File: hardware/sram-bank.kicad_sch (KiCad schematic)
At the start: 13 parts, among them U1 74LVC138A, U13 74LVC138A

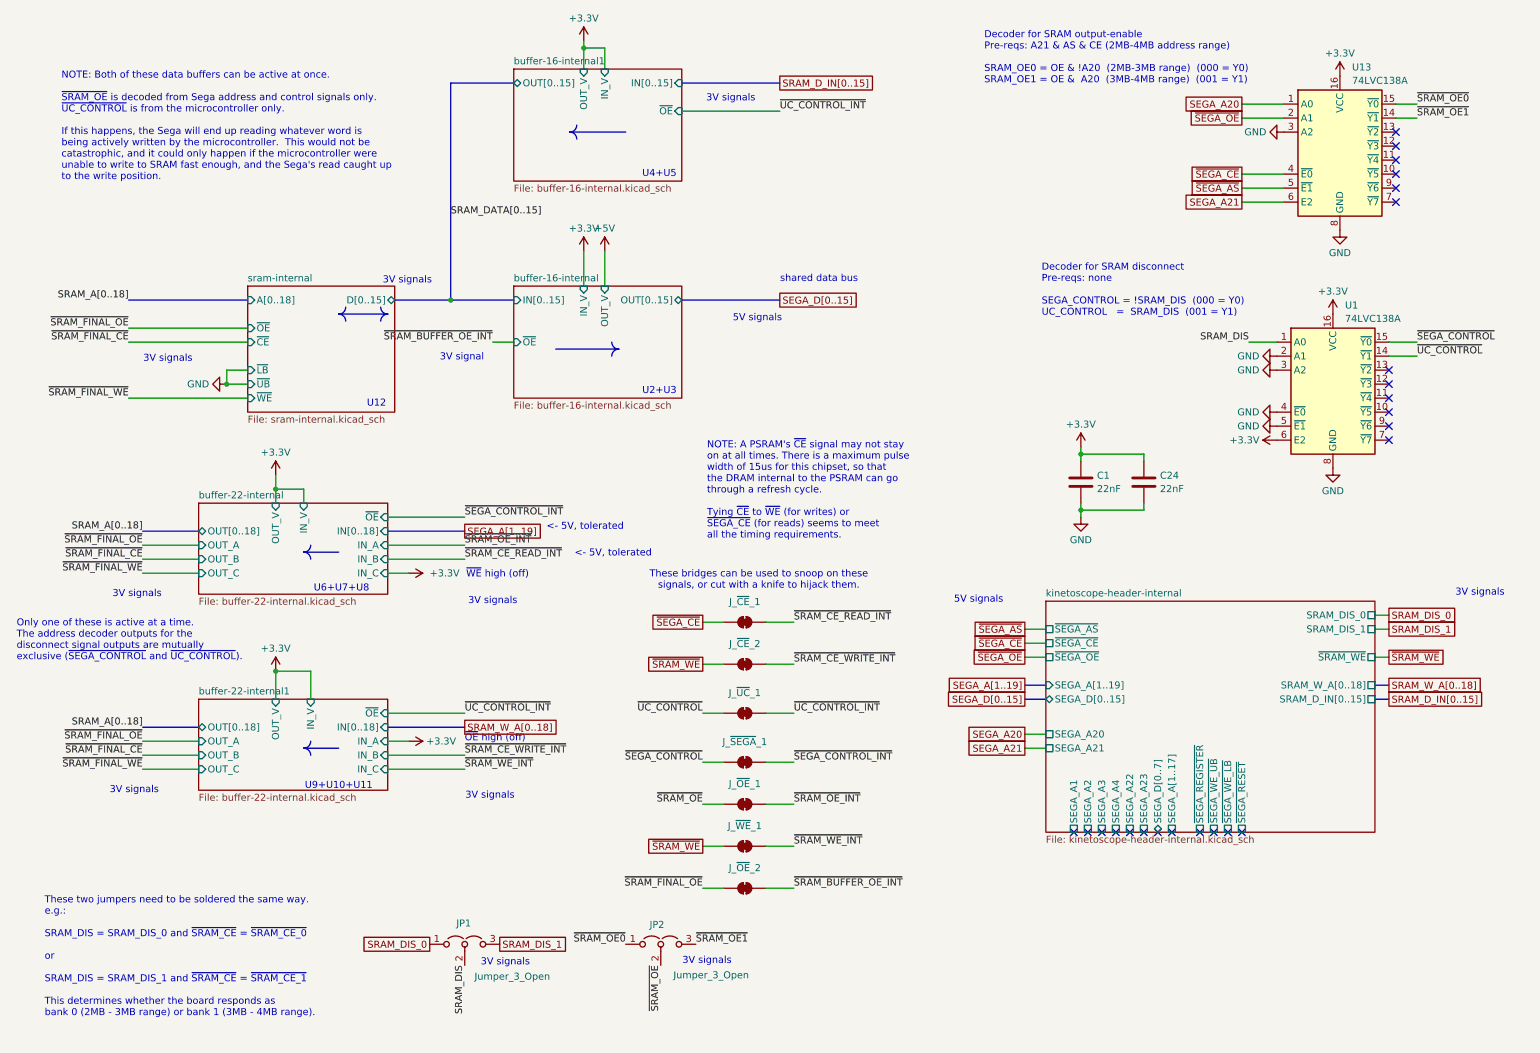
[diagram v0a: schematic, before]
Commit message: Move SRAM bank board design into shareable subsheet
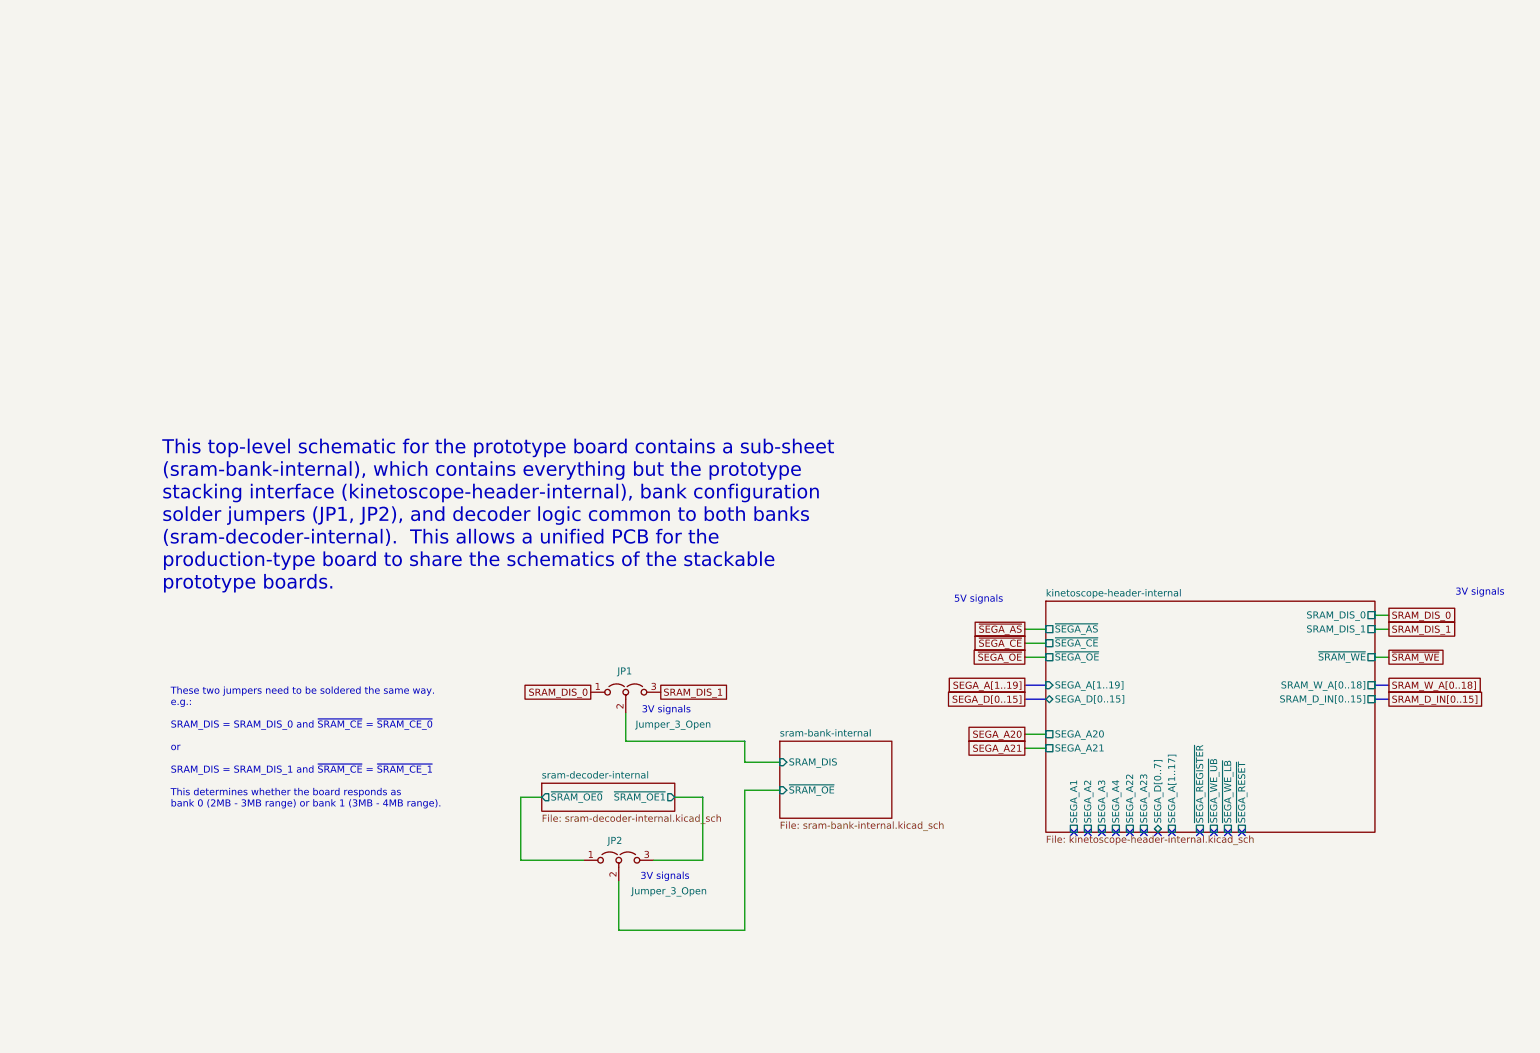
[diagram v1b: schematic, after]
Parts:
- removed C1, C24: 22nF, Capacitor_SMD:C_0603_1608Metric, symbol Device:C
- removed J_~{CE}_1, J_~{CE}_2, J_~{OE}_1, J_~{OE}_2, J_~{SEGA}_1, J_~{UC}_1, J_~{WE}_1: ~, Jumper:SolderJumper-2_P1.3mm_Bridged_RoundedPad1.0x1.5mm, symbol Jumper:SolderJumper_2_Bridged
- removed U1, U13: 74LVC138A, Package_SO:TSSOP-16_4.4x5mm_P0.65mm, symbol 74xx:74HC138
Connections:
- net SRAM_DIS renamed sram-bank-internal/SRAM_DIS
- net ~{SRAM_OE0} renamed sram-decoder-internal/~{SRAM_OE0}
- net ~{SRAM_OE1} renamed sram-decoder-internal/~{SRAM_OE1}
- net ~{SRAM_OE} renamed sram-bank-internal/~{SRAM_OE}
- no-connect marks 24 -> 12
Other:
- removed sheet buffer-16-internal
- removed sheet buffer-16-internal1
- removed sheet buffer-22-internal
- removed sheet buffer-22-internal1
- removed sheet sram-internal
- added sheet sram-bank-internal (sram-bank-internal.kicad_sch)
- added sheet sram-decoder-internal (sram-decoder-internal.kicad_sch)
- note added: "This top-level schematic for the prototype board contains a sub-sheet (sram-bank-internal), which contains everything but the prototype stacking interface (kinetoscope-header-internal), bank configuration solder jumpers (JP1, JP2), and decoder logic common to both banks (sram-decoder-internal). This allows a unified PCB for the production-type board to share the schematics of the stackable protot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"
- note removed: "3V signal"
- note removed: "<- 5V, tolerated"
- note removed: "Decoder for SRAM disconnect Pre-reqs: none SEGA_CONTROL = !SRAM_DIS (000 = Y0) UC_CONTROL = SRAM_DIS (001 = Y1)"
- note removed: "Decoder for SRAM output-enable Pre-reqs: A21 & AS & CE (2MB-4MB address range) SRAM_OE0 = OE & !A20 (2MB-3MB range) (000 = Y0) SRAM_OE1 = OE & A20 (3MB-4MB range) (001 = Y1)"
- note removed: "NOTE: A PSRAM's ~{CE} signal may not stay on at all times. There is a maximum pulse width of 15us for this chipset, so that the DRAM internal to the PSRAM can go through a refresh cycle. Tying ~{CE} to ~{WE} (for writes) or ~{SEGA_CE} (for reads) seems to meet all the timing requirements."
- note removed: "NOTE: Both of these data buffers can be active at once. ~{SRAM_OE} is decoded from Sega address and control signals only. ~{UC_CONTROL} is from the microcontroller only. If this happens, the Sega will end up reading whatever word is being actively written by the microcontroller. This would not be catastrophic, and it could only happen if the microcontroller were unable to write to SRAM fast enoug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"
- note removed: "Only one of these is active at a time. The address decoder outputs for the disconnect signal outputs are mutually exclusive (~{SEGA_CONTROL} and ~{UC_CONTROL})."
- note removed: "These bridges can be used to snoop on these signals, or cut with a knife to hijack them."
- note removed: "U12"
- note removed: "U2+U3"
- note removed: "U4+U5"
- note removed: "U6+U7+U8"
- note removed: "U9+U10+U11"
- note removed: "shared data bus"
- note removed: "~{OE} high (off)"
- note removed: "~{WE} high (off)"
- moved on the sheet: JP1, JP2

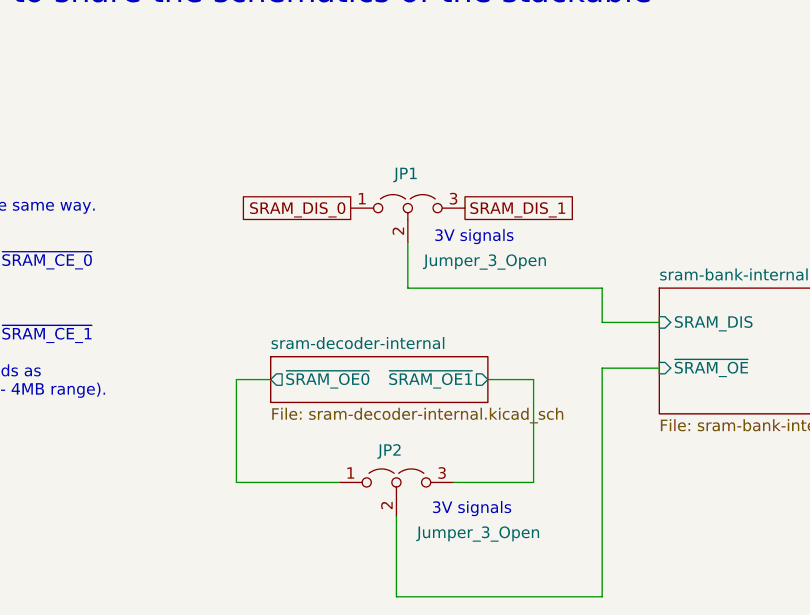
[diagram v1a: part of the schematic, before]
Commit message: Reannotate schematics and drop debug bridges
Parts are now numbered starting at 0 for cart, 100 for SRAM, 300 for
microcontroller.

Also, drop debug bridges that made routing more difficult and had the
same names across prototype boards.

Hopefully this will help avoid naming conflicts for the unified PCB.

Also, redo prototype PCB layouts.

Now that all the names have changed, update board layouts.
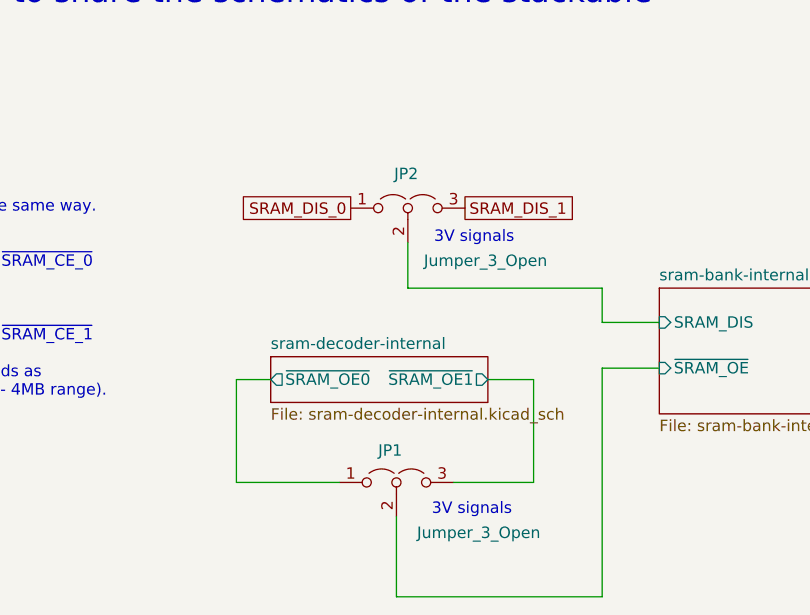
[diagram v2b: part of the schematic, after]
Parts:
- renumbered JP2 to JP1, JP1 to JP2
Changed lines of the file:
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@@
 		(on_board yes)
 		(dnp no)
-		(property "Reference" "JP1"
+		(property "Reference" "JP2"
 			(at 121.666 132.08 0)
 			(effects
@@
 			(project "sram-bank"
 				(path "/620c762c-1ae9-4ea9-ab1a-d023a8da85ac"
-					(reference "JP1")
+					(reference "JP2")
 					(unit 1)
 				)
@@
 		(on_board yes)
 		(dnp no)
-		(property "Reference" "JP2"
+		(property "Reference" "JP1"
 			(at 119.888 162.814 0)
 			(effects
@@
 			(project "sram-bank"
 				(path "/620c762c-1ae9-4ea9-ab1a-d023a8da85ac"
-					(reference "JP2")
+					(reference "JP1")
 					(unit 1)
 				)
